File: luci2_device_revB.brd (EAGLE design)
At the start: 80 x 70.6 mm, 49 parts, among them Q3 IRF9540, Q4 IRF9540

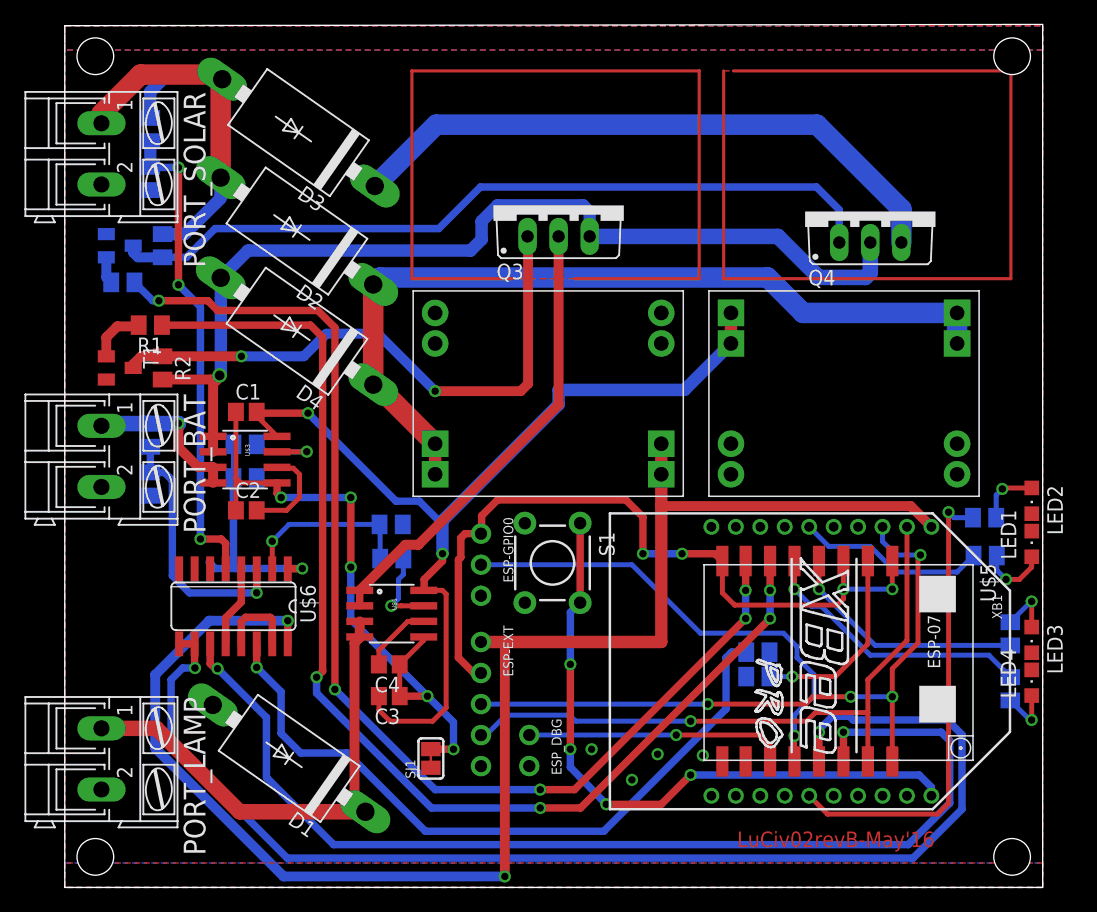
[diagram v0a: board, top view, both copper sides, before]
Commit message: Add route size
this change apply to every route that contain high current
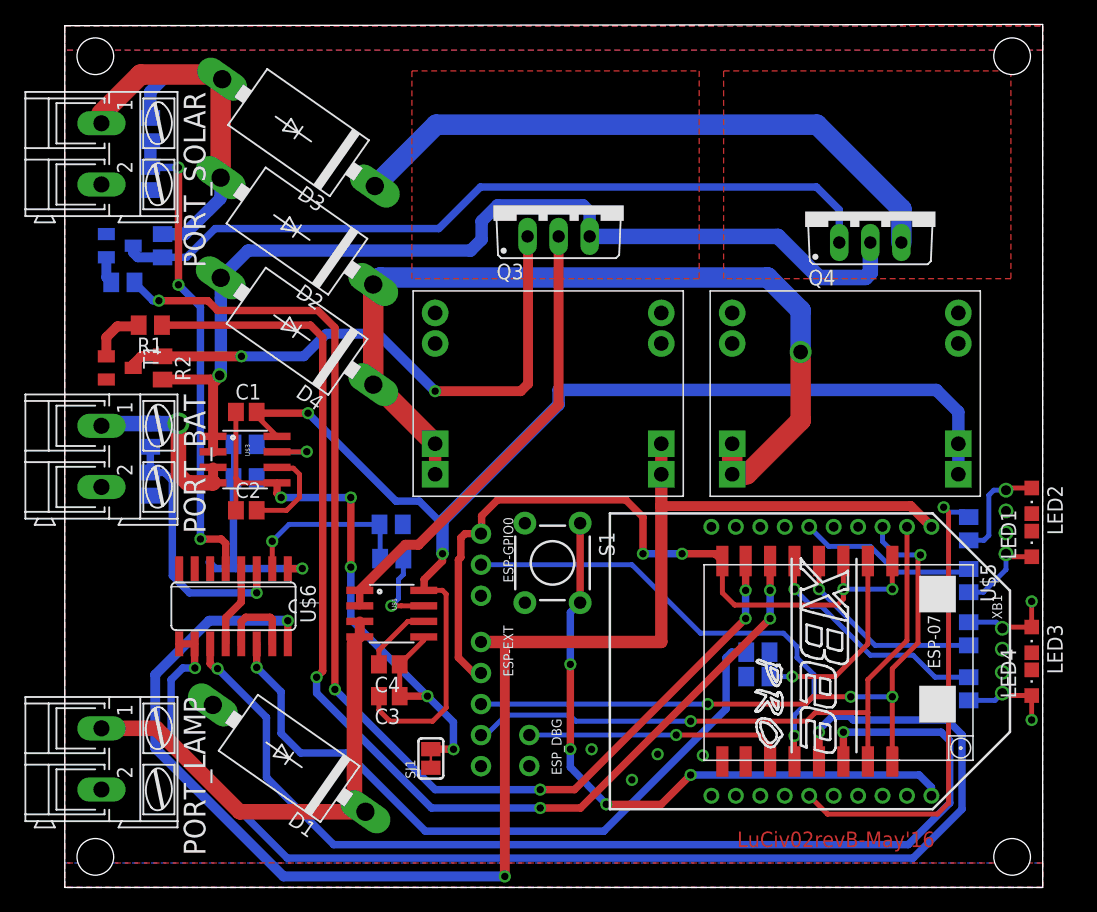
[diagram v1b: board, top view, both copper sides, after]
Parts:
- moved U$2 27.7 mm to (52.8, 32.0), turned to 0 degrees
- moved R11 3.40 mm to (74.0, 20.8)
- moved R12 3.40 mm to (74.0, 16.2)
- moved R4 2.45 mm to (74.0, 25.1), turned to 90 degrees
- moved R3 1.58 mm to (74.0, 29.4), turned to 90 degrees
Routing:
- net Q4_SINK: track 80.2 -> 0.00 mm
- net Q3_SINK: track 75.9 -> 0.00 mm
- net +5V: track 79.4 -> 99.8 mm
- net N$5: track 5.00 -> 8.87 mm
- net N$8: track 69.5 -> 73.0 mm, vias 0 -> 1
- net INDICATOR_1: track 23.0 -> 19.5 mm
- net INDICATOR_0: track 19.9 -> 16.5 mm
- net N$16: track 4.41 -> 7.48 mm, vias 1 -> 2
- net N$15: track 4.55 -> 7.50 mm, vias 1 -> 2
- net VBAT: track 13.1 -> 14.9 mm
- net N$3: track 5.63 -> 7.33 mm
- net XB_RSSI: track 15.5 -> 14.7 mm
- net XB_ASSOC: track 38.4 -> 39.1 mm
- net N$22: track 0.50 -> 0.00 mm
- added copper zone on layer 1, net HEATSINK
- added copper zone on layer 1, net HEATSINK2
- removed copper zone on layer 1, net Q3_SINK
- removed copper zone on layer 1, net Q4_SINK

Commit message: Unroute solved
blah
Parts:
- moved SJ1 1.62 mm to (28.4, 11.2)
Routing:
- net +3V3: track 126.5 -> 123.0 mm
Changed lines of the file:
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@@
 <element name="R5" library="resistor" package="M0805" value="R2K" x="26.7" y="29.7" rot="MR0"/>
 <element name="R6" library="resistor" package="M0805" value="R1K" x="26.75" y="26.9" rot="MR180"/>
-<element name="SJ1" library="microbuilder" package="SOLDERJUMPER_CLOSEDWIRE" value="" x="29.95" y="10.55" rot="R90"/>
+<element name="SJ1" library="microbuilder" package="SOLDERJUMPER_CLOSEDWIRE" value="" x="28.45" y="11.15" rot="R90"/>
 <element name="R13" library="resistor" package="M0805" value="R1K" x="56.7" y="17.25" rot="MR180"/>
 <element name="R14" library="resistor" package="M0805" value="R2K" x="56.7" y="19.25" rot="MR0"/>
@@
 <via x="77" y="30.8" extent="1-16" drill="0.8128"/>
 <via x="77" y="29" extent="1-16" drill="0.8128"/>
-<wire x1="27.65" y1="29.7" x2="15.7" y2="33.5" width="0" layer="19" extent="16-16"/>
+<via x="24" y="37.9" extent="1-16" drill="0.6"/>
+<via x="26.4" y="35.6" extent="1-16" drill="0.6"/>
+<via x="32.4" y="16.3" extent="1-16" drill="0.6"/>
+<via x="32.4" y="13.7" extent="1-16" drill="0.6"/>
 </signal>
 <signal name="CTRL_LAMP">
@@
 <wire x1="18.245" y1="21.82" x2="11.82" y2="21.82" width="0.8128" layer="16"/>
 <wire x1="11.82" y1="21.82" x2="7.4" y2="17.4" width="0.8128" layer="16"/>
-<wire x1="7.4" y1="17.4" x2="7.4" y2="11.4" width="0.8128" layer="16"/>
-<wire x1="7.4" y1="11.4" x2="17.9" y2="0.9" width="0.8128" layer="16"/>
-<wire x1="17.9" y1="0.9" x2="36" y2="0.9" width="0.8128" layer="16"/>
-<via x="36" y="0.9" extent="1-16" drill="0.6"/>
-<wire x1="36" y1="0.9" x2="36" y2="20.08" width="0.8128" layer="1"/>
+<wire x1="7.4" y1="17.4" x2="7.4" y2="8.9" width="0.8128" layer="16"/>
+<wire x1="36" y1="6.4" x2="36" y2="20.08" width="0.8128" layer="1"/>
 <wire x1="70.9" y1="29.5" x2="69.2" y2="31.2" width="0.8128" layer="1"/>
 <wire x1="69.2" y1="31.2" x2="48.8" y2="31.2" width="0.8128" layer="1"/>
+<wire x1="7.4" y1="8.9" x2="8.2" y2="8.1" width="0.8128" layer="16"/>
+<via x="8.2" y="8.1" extent="1-16" drill="0.8" shape="square"/>
+<wire x1="8.2" y1="8.1" x2="13.3" y2="3" width="0.8128" layer="1"/>
+<wire x1="13.3" y1="3" x2="32.6" y2="3" width="0.8128" layer="1"/>
+<wire x1="32.6" y1="3" x2="36" y2="6.4" width="0.8128" layer="1"/>
 </signal>
 <signal name="XB_RSSI">
@@
 <wire x1="29.3662" y1="24.305" x2="30.895" y2="24.305" width="0.4064" layer="1"/>
 <wire x1="30.895" y1="24.305" x2="31.2" y2="24" width="0.4064" layer="1"/>
-<wire x1="31.2" y1="24" x2="31.2" y2="14.7" width="0.4064" layer="1"/>
-<wire x1="31.2" y1="14.7" x2="30.1" y2="13.6" width="0.4064" layer="1"/>
-<wire x1="30.1" y1="13.6" x2="26.6" y2="13.6" width="0.4064" layer="1"/>
+<wire x1="31.2" y1="24" x2="31.2" y2="15.3" width="0.4064" layer="1"/>
+<wire x1="31.2" y1="15.3" x2="29.5" y2="13.6" width="0.4064" layer="1"/>
+<wire x1="29.5" y1="13.6" x2="26.6" y2="13.6" width="0.4064" layer="1"/>
 <wire x1="26.6" y1="13.6" x2="25.7" y2="14.5" width="0.4064" layer="1"/>
 <wire x1="25.7" y1="14.5" x2="25.7" y2="15.65" width="0.4064" layer="1"/>
@@
 <wire x1="27.4" y1="15.65" x2="29.67" y2="15.65" width="0.6096" layer="1"/>
 <via x="29.67" y="15.65" extent="1-16" drill="0.6"/>
-<wire x1="29.67" y1="15.65" x2="31.8" y2="13.52" width="0.6096" layer="16"/>
-<wire x1="31.8" y1="13.52" x2="31.8" y2="11.3" width="0.6096" layer="16"/>
-<via x="31.8" y="11.3" extent="1-16" drill="0.6"/>
-<wire x1="31.8" y1="11.3" x2="31.788" y2="11.312" width="0.6096" layer="1"/>
-<wire x1="31.788" y1="11.312" x2="29.95" y2="11.312" width="0.6096" layer="1"/>
+<wire x1="29.67" y1="15.65" x2="31.1" y2="14.22" width="0.6096" layer="16"/>
+<wire x1="31.1" y1="14.22" x2="31.1" y2="11.9" width="0.6096" layer="16"/>
+<via x="31.1" y="11.9" extent="1-16" drill="0.6"/>
+<wire x1="31.1" y1="11.9" x2="31.088" y2="11.912" width="0.6096" layer="1"/>
+<wire x1="31.088" y1="11.912" x2="28.45" y2="11.912" width="0.6096" layer="1"/>
 <wire x1="17.3662" y1="33.095" x2="17.3662" y2="32.2338" width="0.6096" layer="1"/>
 <wire x1="17.3662" y1="32.2338" x2="17.7" y2="31.9" width="0.6096" layer="1"/>
